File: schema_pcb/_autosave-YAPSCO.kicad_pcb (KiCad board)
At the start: 2 copper layers, 82.8 x 73.2 mm, 78 parts, among them J2 DB9_Female_MountingHoles, K1 Supply, K3 FautlPol, P1 STEP, P2 DIR, P3 CONN, P4 ENABLE, P5 +-10V, P6 InOut, Q1 NPN, U1 7805, U10 MC33063AD, U2 dsPIC30F4012, U3 6N137, U4 6N137, U5 6N137, U6 LM358, U7 74HC14, U8 LM339D, U9 L7812

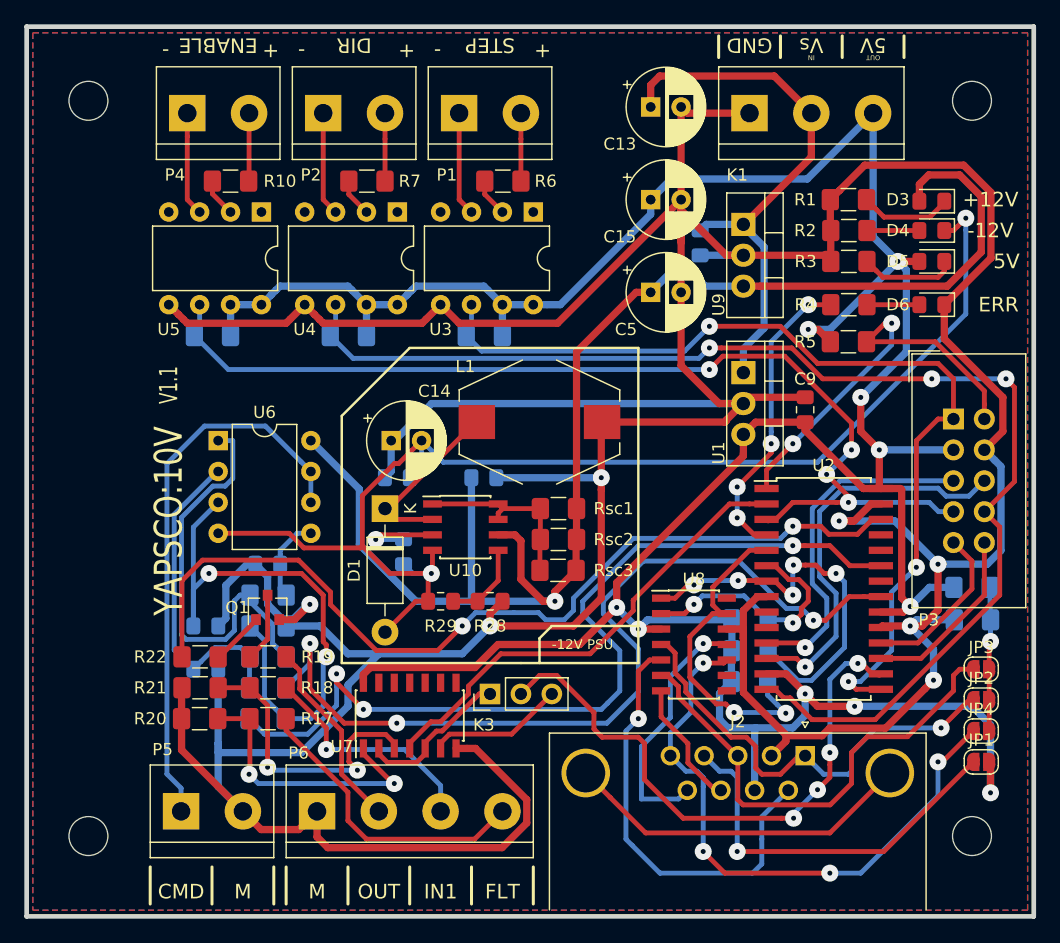
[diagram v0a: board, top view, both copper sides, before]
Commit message: Feedback changed to cheap linear scale
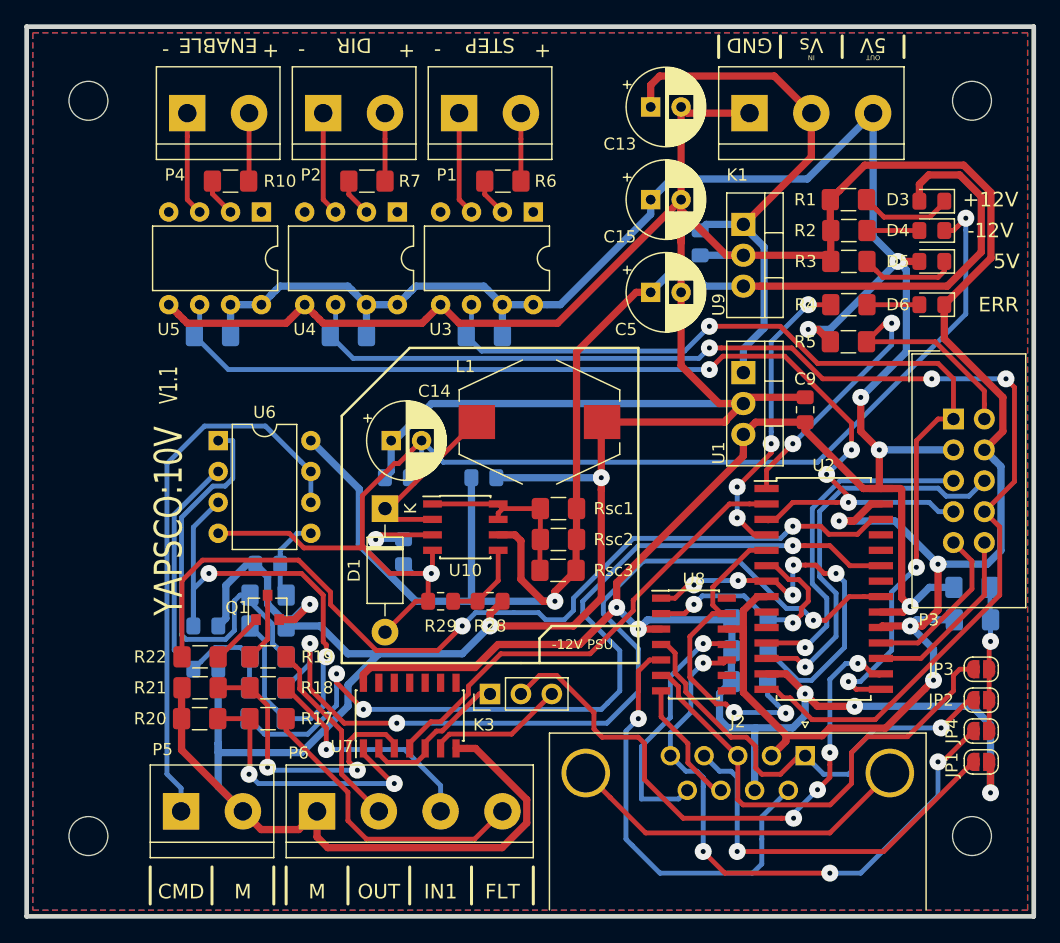
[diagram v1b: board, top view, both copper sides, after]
